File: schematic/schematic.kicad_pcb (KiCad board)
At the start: 2 copper layers, 7 parts, among them U1 STM32H743VITx

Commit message: 1%
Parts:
- added C10: 100nF, Capacitor_SMD:C_0805_2012Metric, F.Cu at (161.4, 97.0)
- added C11: 1uF, Capacitor_SMD:C_0805_2012Metric, F.Cu at (161.4, 100.0)
- added C12: 2.2uF, Capacitor_SMD:C_0805_2012Metric, F.Cu at (161.4, 103.0)
- added C13: 2.2uF, Capacitor_SMD:C_0805_2012Metric, F.Cu at (161.4, 106.0)
- added C7: 100nF, Capacitor_SMD:C_0805_2012Metric, F.Cu at (161.4, 88.0)
- added C8: 100nF, Capacitor_SMD:C_0805_2012Metric, F.Cu at (161.4, 91.0)
- added C9: 100nF, Capacitor_SMD:C_0805_2012Metric, F.Cu at (161.4, 94.0)
- C1, C3, C4, C5: value C -> 100nF
- C2: value 104 -> 100nF
- C6: value C -> 4.7uF
- moved C1 64.2 mm to (169.1, 88.5)
- moved C2 64.2 mm to (169.1, 91.5)
- moved C3 64.2 mm to (169.1, 94.5)
- moved C4 64.2 mm to (169.1, 97.5)
- moved C5 64.2 mm to (169.1, 100.5)
- moved C6 64.2 mm to (169.1, 103.5)
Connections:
- U1 pad 100: GND -> +3V3
- U1 pad 11: GND -> +3V3
- U1 pad 14: unconnected-(U1-NRST-Pad14) -> /NRST
- U1 pad 19: unconnected-(U1-VSSA-Pad19) -> GND
- U1 pad 20: unconnected-(U1-VREF+-Pad20) -> +3V3
- U1 pad 21: unconnected-(U1-VDDA-Pad21) -> +3V3
- U1 pad 27: GND -> +3V3
- U1 pad 48: unconnected-(U1-VCAP-Pad48) -> Net-(C12-Pad1)
- U1 pad 50: GND -> +3V3
- U1 pad 6: unconnected-(U1-VBAT-Pad6) -> +3V3
- U1 pad 73: unconnected-(U1-VCAP-Pad73) -> Net-(C13-Pad1)
- U1 pad 75: GND -> +3V3
- U1 pad 94: unconnected-(U1-BOOT0-Pad94) -> GND

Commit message: vẽ xong phần cơ bản
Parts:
- added C14: 100nF, Capacitor_SMD:C_0805_2012Metric, F.Cu at (161.1, 112.0)
- added C15: 0.1uF, Capacitor_SMD:C_0805_2012Metric, F.Cu at (166.6, 135.4)
- added C16: C, Capacitor_SMD:C_0805_2012Metric, F.Cu at (172.6, 110.0)
- added C17: C, Capacitor_SMD:C_0805_2012Metric, F.Cu at (172.6, 113.0)
- added J1: Conn_ARM_SWD_TagConnect_TC2030-NL, Connector:Tag-Connect_TC2030-IDC-NL_2x03_P1.27mm_Vertical, F.Cu at (170.5, 129.0)
- added R1: 10K, Resistor_SMD:R_0805_2012Metric, F.Cu at (142.6, 114.5)
- added R2: 10K, Resistor_SMD:R_0805_2012Metric, F.Cu at (169.6, 135.4)
- added R3: 10K, Resistor_SMD:R_0805_2012Metric, F.Cu at (172.5, 135.4)
- added SW1: SW_Push, Button_Switch_SMD:SW_Push_1P1T_NO_6x6mm_H9.5mm, F.Cu at (142.5, 134.5)
- added Y1: Crystal_GND23_Small, Crystal:Crystal_SMD_EuroQuartz_MJ-4Pin_5.0x3.2mm_HandSoldering, F.Cu at (139.7, 83.6)
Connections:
- U1 pad 12: unconnected-(U1-PH0-Pad12) -> /PH0
- U1 pad 13: unconnected-(U1-PH1-Pad13) -> /PH1
- U1 pad 72: unconnected-(U1-PA13-Pad72) -> /SWDIO
- U1 pad 76: unconnected-(U1-PA14-Pad76) -> /SWCLK
- U1 pad 94: GND -> Net-(U1-BOOT0)

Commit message: no message
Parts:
- added U2: AMS1117, Package_TO_SOT_SMD:SOT-223-3_TabPin2, F.Cu at (158.3, 74.5)
- added U4: MP1584, MP1584:SO-08POWER, F.Cu at (142.5, 71.0)

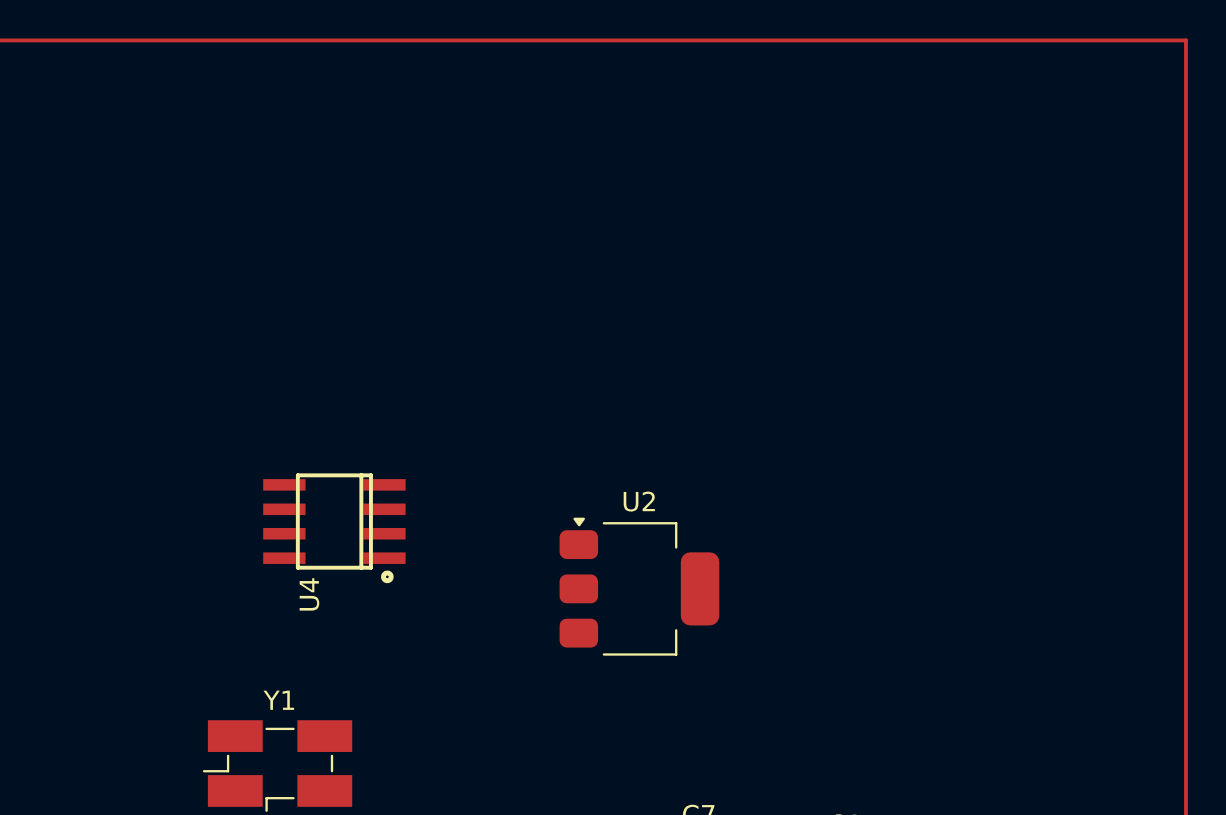
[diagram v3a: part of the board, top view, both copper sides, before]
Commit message: thêm phần driver tb66, ve phần nguồn 5v
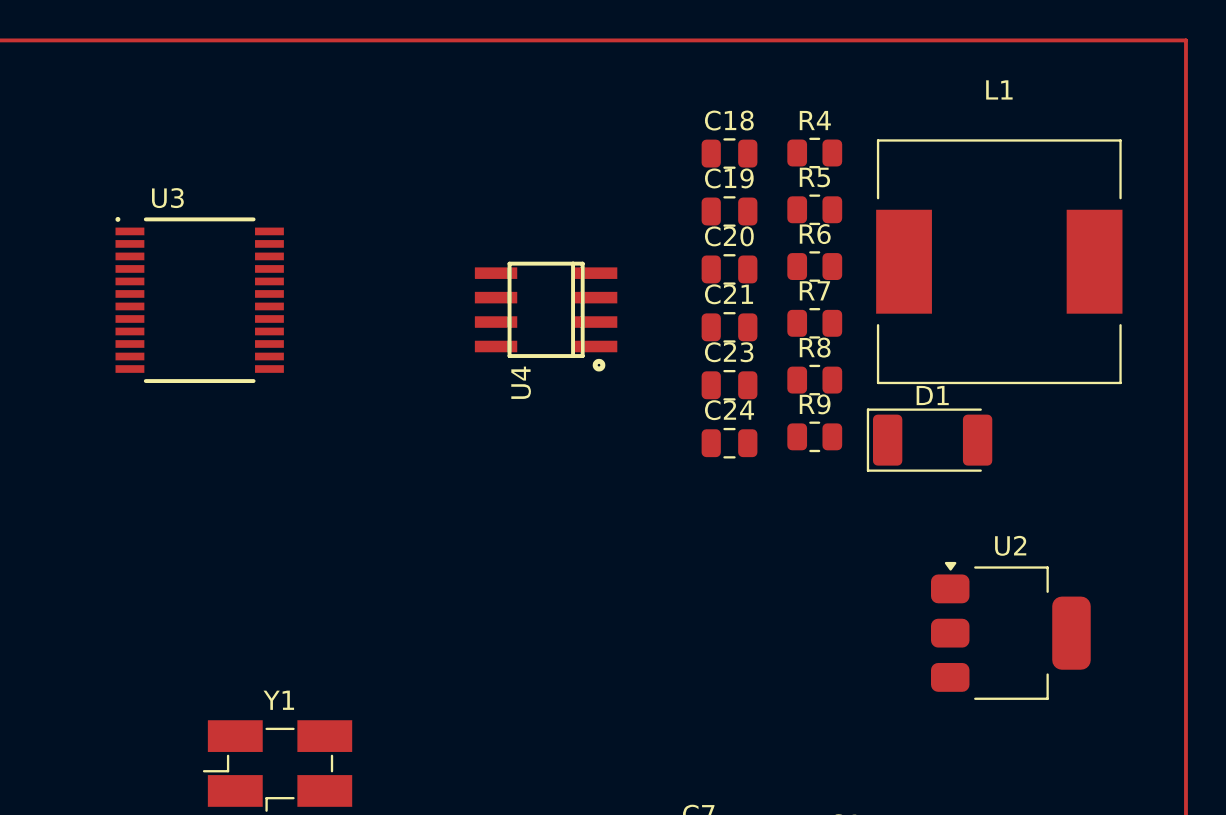
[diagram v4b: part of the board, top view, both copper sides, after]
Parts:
- added C18: 22uF, Capacitor_SMD:C_0805_2012Metric, F.Cu at (163.0, 51.9)
- added C19: 10uF, Capacitor_SMD:C_0805_2012Metric, F.Cu at (163.0, 54.9)
- added C20: 100nF, Capacitor_SMD:C_0805_2012Metric, F.Cu at (163.0, 57.9)
- added C21: 150pF, Capacitor_SMD:C_0805_2012Metric, F.Cu at (163.0, 60.9)
- added C23: 10uF, Capacitor_SMD:C_0805_2012Metric, F.Cu at (163.0, 63.9)
- added C24: 10uF, Capacitor_SMD:C_0805_2012Metric, F.Cu at (163.0, 66.9)
- added D1: 40V-3A, Diode_SMD:D_2010_5025Metric_Pad1.52x2.65mm_HandSolder, F.Cu at (173.6, 66.8)
- added L1: 15uH, Inductor_SMD:L_12x12mm_H4.5mm, F.Cu at (177.1, 57.5)
- added R4: 210K, Resistor_SMD:R_0805_2012Metric, F.Cu at (167.5, 51.9)
- added R5: 40.2K, Resistor_SMD:R_0805_2012Metric, F.Cu at (167.5, 54.8)
- added R6: 100k, Resistor_SMD:R_0805_2012Metric, F.Cu at (167.5, 57.8)
- added R7: 100K, Resistor_SMD:R_0805_2012Metric, F.Cu at (167.5, 60.7)
- added R8: 67k, Resistor_SMD:R_0805_2012Metric, F.Cu at (167.5, 63.6)
- added R9: 20k, Resistor_SMD:R_0805_2012Metric, F.Cu at (167.5, 66.6)
- added U3: TB6612FNG_C_8_EL, Library:SOP65P760X160-24N, F.Cu at (135.5, 59.5)
- moved U2 19.4 mm to (177.7, 76.8)
- moved U4 15.6 mm to (153.5, 60.0)
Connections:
- U1 pad 87: unconnected-(U1-PD6-Pad87) -> /BIN1
- U1 pad 88: unconnected-(U1-PD7-Pad88) -> /BIN2
- U1 pad 91: unconnected-(U1-PB5-Pad91) -> /AIN1
- U1 pad 92: unconnected-(U1-PB6-Pad92) -> /AIN2
- U4 pad 2: unconnected-(U4-EN-Pad2) -> Net-(U4-EN)
- U4 pad 3: unconnected-(U4-COMP-Pad3) -> Net-(U4-COMP)
- U4 pad 5: unconnected-(U4-GND-Pad5) -> GND
- U4 pad 6: unconnected-(U4-FREQ-Pad6) -> Net-(U4-FREQ)
- U4 pad 7: unconnected-(U4-VIN-Pad7) -> 6-7.5V
- U4 pad 8: unconnected-(U4-BST-Pad8) -> Net-(U4-BST)

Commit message: no message
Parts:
- added C22: 100nF, Capacitor_SMD:C_0603_1608Metric, F.Cu at (150.7, 73.0)
- added C25: 10uF, Capacitor_SMD:C_0603_1608Metric, F.Cu at (150.7, 75.5)
- added C26: 10uF, Capacitor_SMD:C_0603_1608Metric, F.Cu at (150.7, 78.0)
- added C27: 100nF, Capacitor_SMD:C_0603_1608Metric, F.Cu at (150.7, 80.5)
- C1, C10, C11, C12, C13, C14, C15, C18, C19, C2, C20, C24, C3, C4, C5, C6, C7, C8, C9: footprint Capacitor_SMD:C_0805_2012Metric -> Capacitor_SMD:C_0603_1608Metric
- C16, C17: value C -> 15pF; footprint Capacitor_SMD:C_0805_2012Metric -> Capacitor_SMD:C_0603_1608Metric
- D1: value 40V-3A -> 40V-5A; footprint Diode_SMD:D_2010_5025Metric_Pad1.52x2.65mm_HandSolder -> Diode_SMD:D_SMA
- L1: footprint Inductor_SMD:L_12x12mm_H4.5mm -> Inductor_SMD:L_7.3x7.3_H4.5
- R1, R2, R3, R4, R6, R7: footprint Resistor_SMD:R_0805_2012Metric -> Resistor_SMD:R_0603_1608Metric
- R8: value 67k -> 63.4K
- SW1: footprint Button_Switch_SMD:SW_Push_1P1T_NO_6x6mm_H9.5mm -> Button_Switch_SMD:SW_Push_1P1T_NO_CK_KSC6xxJ
- moved U2 12.0 mm to (166.0, 79.5), turned to -90 degrees
- moved Y1 8.55 mm to (131.3, 85.4)
- moved U4 3.00 mm to (153.5, 57.0)
- turned SW1 to 0 degrees
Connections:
- U1 pad 22: unconnected-(U1-PA0-Pad22) -> /Encoder_A_R
- U1 pad 23: unconnected-(U1-PA1-Pad23) -> /Encoder_B_R
- U1 pad 29: unconnected-(U1-PA5-Pad29) -> /Encoder_A_L
- U1 pad 30: unconnected-(U1-PA6-Pad30) -> /sensorFF
- U1 pad 31: unconnected-(U1-PA7-Pad31) -> /sensorFR
- U1 pad 32: unconnected-(U1-PC4-Pad32) -> /sensorFL
- U1 pad 33: unconnected-(U1-PC5-Pad33) -> /sensorR
- U1 pad 35: unconnected-(U1-PB1-Pad35) -> /sensorL
- U1 pad 39: unconnected-(U1-PE9-Pad39) -> /PWMA
- U1 pad 41: unconnected-(U1-PE11-Pad41) -> /PWMB
- U1 pad 46: unconnected-(U1-PB10-Pad46) -> /UART3_TX
- U1 pad 47: unconnected-(U1-PB11-Pad47) -> /UART3_RX
- U1 pad 53: unconnected-(U1-PB14-Pad53) -> /UART1_TX
- U1 pad 54: unconnected-(U1-PB15-Pad54) -> /UART1_RX
- U1 pad 89: unconnected-(U1-PB3-Pad89) -> /Encoder_B_L
- U3 pad 1: unconnected-(U3-AO1@1-Pad1) -> Net-(U3-AO1@1)
- U3 pad 11: unconnected-(U3-BO1@1-Pad11) -> Net-(U3-BO1@1)
- U3 pad 12: unconnected-(U3-BO1@2-Pad12) -> Net-(U3-BO1@1)
- U3 pad 15: unconnected-(U3-PWMB-Pad15) -> /PWMB
- U3 pad 2: unconnected-(U3-AO1@2-Pad2) -> Net-(U3-AO1@1)
- U3 pad 23: unconnected-(U3-PWMA-Pad23) -> /PWMA
- U3 pad 5: unconnected-(U3-AO2@1-Pad5) -> Net-(U3-AO2@1)
- U3 pad 6: unconnected-(U3-AO2@2-Pad6) -> Net-(U3-AO2@1)
- U3 pad 7: unconnected-(U3-BO2@1-Pad7) -> Net-(U3-BO2@1)
- U3 pad 8: unconnected-(U3-BO2@2-Pad8) -> Net-(U3-BO2@1)

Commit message: xong phần nguồn
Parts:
- R8: value 63.4K -> 75k
- moved C16 45.0 mm to (129.3, 97.5)
- moved C17 45.0 mm to (129.3, 100.5)
- moved C11 15.9 mm to (176.7, 104.5)
- moved C8 15.9 mm to (176.7, 95.5)
- moved C10 15.9 mm to (176.7, 101.5)
- moved C12 15.9 mm to (176.7, 107.5)
- moved C13 15.9 mm to (176.7, 110.5)
- moved C7 15.9 mm to (176.7, 92.4)
- moved C9 15.9 mm to (176.7, 98.5)
- moved C2 13.4 mm to (181.2, 97.0)
- moved C3 13.4 mm to (181.2, 100.0)
- moved C5 13.4 mm to (181.2, 106.0)
- moved C6 13.4 mm to (181.2, 109.0)
- moved C1 13.4 mm to (181.2, 94.0)
- moved C4 13.4 mm to (181.2, 103.0)
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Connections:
- net 6-7.5V renamed 6.5-7.5V
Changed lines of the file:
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@@
 	(net 82 "/PH0")
 	(net 83 "+5V")
-	(net 84 "6-7.5V")
+	(net 84 "6.5-7.5V")
 	(net 85 "Net-(U4-BST)")
 	(net 86 "Net-(C21-Pad2)")
@@
 			(layers "F.Cu" "F.Paste" "F.Mask")
 			(roundrect_rratio 0.25)
-			(net 84 "6-7.5V")
+			(net 84 "6.5-7.5V")
 			(pintype "passive")
 		)
@@
 	(footprint "Capacitor_SMD:C_0603_1608Metric"
 		(layer "F.Cu")
-		(at 172.55 113)
+		(at 129.275 100.51)
 		(descr "Capacitor SMD 0603 (1608 Metric), square (rectangular) end terminal, IPC_7351 nominal, (Body size source: IPC-SM-782 page 76, https://www.pcb-3d.com/wordpress/wp-content/uploads/ipc-sm-782a_amendment_1_and_2.pdf), generated with kicad-footprint-generator")
 		(tags "capacitor")
@@
 	(footprint "Resistor_SMD:R_0603_1608Metric"
 		(layer "F.Cu")
-		(at 142.5875 114.5)
+		(at 137.325 113)
 		(descr "Resistor SMD 0603 (1608 Metric), square (rectangular) end terminal, IPC_7351 nominal, (Body size source: IPC-SM-782 page 72, https://www.pcb-3d.com/wordpress/wp-content/uploads/ipc-sm-782a_amendment_1_and_2.pdf), generated with kicad-footprint-generator")
 		(tags "resistor")
@@
 	(footprint "Capacitor_SMD:C_0603_1608Metric"
 		(layer "F.Cu")
-		(at 172.55 109.99)
+		(at 129.275 97.5)
 		(descr "Capacitor SMD 0603 (1608 Metric), square (rectangular) end terminal, IPC_7351 nominal, (Body size source: IPC-SM-782 page 76, https://www.pcb-3d.com/wordpress/wp-content/uploads/ipc-sm-782a_amendment_1_and_2.pdf), generated with kicad-footprint-generator")
 		(tags "capacitor")
@@
 	(footprint "Capacitor_SMD:C_0603_1608Metric"
 		(layer "F.Cu")
-		(at 161.45 96.98)
+		(at 176.725 101.47)
 		(descr "Capacitor SMD 0603 (1608 Metric), square (rectangular) end terminal, IPC_7351 nominal, (Body size source: IPC-SM-782 page 76, https://www.pcb-3d.com/wordpress/wp-content/uploads/ipc-sm-782a_amendment_1_and_2.pdf), generated with kicad-footprint-generator")
 		(tags "capacitor")
@@
 	(footprint "Capacitor_SMD:C_0603_1608Metric"
 		(layer "F.Cu")
-		(at 169.05 88.45)
+		(at 181.225 93.99)
 		(descr "Capacitor SMD 0603 (1608 Metric), square (rectangular) end terminal, IPC_7351 nominal, (Body size source: IPC-SM-782 page 76, https://www.pcb-3d.com/wordpress/wp-content/uploads/ipc-sm-782a_amendment_1_and_2.pdf), generated with kicad-footprint-generator")
 		(tags "capacitor")
@@
 	(footprint "Crystal:Crystal_SMD_EuroQuartz_MJ-4Pin_5.0x3.2mm_HandSoldering"
 		(layer "F.Cu")
-		(at 131.325 85.425)
+		(at 139.825 84.425)
 		(descr "SMD Crystal EuroQuartz MJ series http://cdn-reichelt.de/documents/datenblatt/B400/MJ.pdf, hand-soldering, 5.0x3.2mm^2 package")
 		(tags "SMD SMT crystal hand-soldering")
@@
 			)
 		)
-		(property "Value" "63.4K"
+		(property "Value" "75k"
 			(at 0 1.65 0)
 			(layer "F.Fab")
@@
 			(layers "F.Cu" "F.Paste" "F.Mask")
 			(roundrect_rratio 0.243902)
-			(net 84 "6-7.5V")
+			(net 84 "6.5-7.5V")
 			(pintype "passive")
 		)
@@
 	(footprint "Capacitor_SMD:C_0603_1608Metric"
 		(layer "F.Cu")
-		(at 161.45 106.01)
+		(at 176.725 110.5)
 		(descr "Capacitor SMD 0603 (1608 Metric), square (rectangular) end terminal, IPC_7351 nominal, (Body size source: IPC-SM-782 page 76, https://www.pcb-3d.com/wordpress/wp-content/uploads/ipc-sm-782a_amendment_1_and_2.pdf), generated with kicad-footprint-generator")
 		(tags "capacitor")
@@
 		)
 		(property "Value" "2.2uF"
-			(at 0 1.43 0)
+			(at -43.275 -11.06 0)
 			(layer "F.Fab")
 			(effects
@@
 	(footprint "Capacitor_SMD:C_0603_1608Metric"
 		(layer "F.Cu")
-		(at 161.45 90.96)
+		(at 176.725 95.45)
 		(descr "Capacitor SMD 0603 (1608 Metric), square (rectangular) end terminal, IPC_7351 nominal, (Body size source: IPC-SM-782 page 76, https://www.pcb-3d.com/wordpress/wp-content/uploads/ipc-sm-782a_amendment_1_and_2.pdf), generated with kicad-footprint-generator")
 		(tags "capacitor")
@@
 	(footprint "Capacitor_SMD:C_0603_1608Metric"
 		(layer "F.Cu")
-		(at 161.45 93.97)
+		(at 176.725 98.46)
 		(descr "Capacitor SMD 0603 (1608 Metric), square (rectangular) end terminal, IPC_7351 nominal, (Body size source: IPC-SM-782 page 76, https://www.pcb-3d.com/wordpress/wp-content/uploads/ipc-sm-782a_amendment_1_and_2.pdf), generated with kicad-footprint-generator")
 		(tags "capacitor")
@@
 	(footprint "Package_TO_SOT_SMD:SOT-223-3_TabPin2"
 		(layer "F.Cu")
-		(at 166 79.5 -90)
+		(at 163.5 89.5 -90)
 		(descr "module CMS SOT223 4 pins")
 		(tags "CMS SOT")
@@
 		)
 		(fp_text user "${REFERENCE}"
-			(at 0 0 360)
+			(at 0 0 0)
 			(layer "F.Fab")
 			(effects
@@
 	(footprint "Capacitor_SMD:C_0603_1608Metric"
 		(layer "F.Cu")
-		(at 161.45 99.99)
+		(at 176.725 104.48)
 		(descr "Capacitor SMD 0603 (1608 Metric), square (rectangular) end terminal, IPC_7351 nominal, (Body size source: IPC-SM-782 page 76, https://www.pcb-3d.com/wordpress/wp-content/uploads/ipc-sm-782a_amendment_1_and_2.pdf), generated with kicad-footprint-generator")
 		(tags "capacitor")
@@
 	(footprint "Capacitor_SMD:C_0603_1608Metric"
 		(layer "F.Cu")
-		(at 161.45 103)
+		(at 176.725 107.49)
 		(descr "Capacitor SMD 0603 (1608 Metric), square (rectangular) end terminal, IPC_7351 nominal, (Body size source: IPC-SM-782 page 76, https://www.pcb-3d.com/wordpress/wp-content/uploads/ipc-sm-782a_amendment_1_and_2.pdf), generated with kicad-footprint-generator")
 		(tags "capacitor")
@@
 	(footprint "Capacitor_SMD:C_0603_1608Metric"
 		(layer "F.Cu")
-		(at 169.05 97.48)
+		(at 181.225 103.02)
 		(descr "Capacitor SMD 0603 (1608 Metric), square (rectangular) end terminal, IPC_7351 nominal, (Body size source: IPC-SM-782 page 76, https://www.pcb-3d.com/wordpress/wp-content/uploads/ipc-sm-782a_amendment_1_and_2.pdf), generated with kicad-footprint-generator")
 		(tags "capacitor")
@@
 	(footprint "Diode_SMD:D_SMA"
 		(layer "F.Cu")
-		(at 173.585 66.77)
+		(at 177.5 67.5)
 		(descr "Diode SMA (DO-214AC)")
 		(tags "Diode SMA (DO-214AC)")
@@
 	(footprint "Capacitor_SMD:C_0603_1608Metric"
 		(layer "F.Cu")
-		(at 169.05 100.49)
+		(at 181.225 106.03)
 		(descr "Capacitor SMD 0603 (1608 Metric), square (rectangular) end terminal, IPC_7351 nominal, (Body size source: IPC-SM-782 page 76, https://www.pcb-3d.com/wordpress/wp-content/uploads/ipc-sm-782a_amendment_1_and_2.pdf), generated with kicad-footprint-generator")
 		(tags "capacitor")
@@
 	(footprint "Capacitor_SMD:C_0603_1608Metric"
 		(layer "F.Cu")
-		(at 161.45 87.95)
+		(at 176.725 92.44)
 		(descr "Capacitor SMD 0603 (1608 Metric), square (rectangular) end terminal, IPC_7351 nominal, (Body size source: IPC-SM-782 page 76, https://www.pcb-3d.com/wordpress/wp-content/uploads/ipc-sm-782a_amendment_1_and_2.pdf), generated with kicad-footprint-generator")
 		(tags "capacitor")
@@
 	(footprint "Capacitor_SMD:C_0603_1608Metric"
 		(layer "F.Cu")
-		(at 169.05 94.47)
+		(at 181.225 100.01)
 		(descr "Capacitor SMD 0603 (1608 Metric), square (rectangular) end terminal, IPC_7351 nominal, (Body size source: IPC-SM-782 page 76, https://www.pcb-3d.com/wordpress/wp-content/uploads/ipc-sm-782a_amendment_1_and_2.pdf), generated with kicad-footprint-generator")
 		(tags "capacitor")
@@
 			(size 0.6 2.2)
 			(layers "F.Cu" "F.Paste" "F.Mask")
-			(net 84 "6-7.5V")
+			(net 84 "6.5-7.5V")
 			(pinfunction "VIN")
 			(pintype "input")
@@
 	(footprint "Package_QFP:LQFP-100_14x14mm_P0.5mm"
 		(layer "F.Cu")
-		(at 142.325 99)
+		(at 142 99)
 		(descr "LQFP, 100 Pin (https://www.nxp.com/docs/en/package-information/SOT407-1.pdf), generated with kicad-footprint-generator ipc_gullwing_generator.py")
 		(tags "LQFP QFP")
@@
 	(footprint "Capacitor_SMD:C_0603_1608Metric"
 		(layer "F.Cu")
-		(at 169.05 103.5)
+		(at 181.225 109.04)
 		(descr "Capacitor SMD 0603 (1608 Metric), square (rectangular) end terminal, IPC_7351 nominal, (Body size source: IPC-SM-782 page 76, https://www.pcb-3d.com/wordpress/wp-content/uploads/ipc-sm-782a_amendment_1_and_2.pdf), generated with kicad-footprint-generator")
 		(tags "capacitor")
@@
 	(footprint "Capacitor_SMD:C_0603_1608Metric"
 		(layer "F.Cu")
-		(at 169.05 91.46)
+		(at 181.225 97)
 		(descr "Capacitor SMD 0603 (1608 Metric), square (rectangular) end terminal, IPC_7351 nominal, (Body size source: IPC-SM-782 page 76, https://www.pcb-3d.com/wordpress/wp-content/uploads/ipc-sm-782a_amendment_1_and_2.pdf), generated with kicad-footprint-generator")
 		(tags "capacitor")
@@
 	(footprint "Capacitor_SMD:C_0603_1608Metric"
 		(layer "F.Cu")
-		(at 161.05 112)
+		(at 159.875 125.05)
 		(descr "Capacitor SMD 0603 (1608 Metric), square (rectangular) end terminal, IPC_7351 nominal, (Body size source: IPC-SM-782 page 76, https://www.pcb-3d.com/wordpress/wp-content/uploads/ipc-sm-782a_amendment_1_and_2.pdf), generated with kicad-footprint-generator")
 		(tags "capacitor")

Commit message: no message
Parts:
- removed J1: Conn_ARM_SWD_TagConnect_TC2030-NL, Connector:Tag-Connect_TC2030-IDC-NL_2x03_P1.27mm_Vertical
- added J2: Conn_01x04_Socket, Connector_JST:JST_PH_B4B-PH-K_1x04_P2.00mm_Vertical, F.Cu at (168.0, 128.0)
- moved U4 34.0 mm to (176.0, 82.5)
- moved R5 27.6 mm to (183.9, 77.0)
- moved R6 27.6 mm to (183.9, 80.0)
- moved R7 27.6 mm to (183.9, 82.9)
- moved R9 27.6 mm to (183.9, 88.8)
- moved R4 27.6 mm to (183.9, 74.0)
- moved R8 27.6 mm to (183.9, 85.8)
